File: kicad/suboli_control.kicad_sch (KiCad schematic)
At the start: 41 parts, among them J1 DC barrel jack panel header 5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, J2 3.5 mm TRS input panel header, J3 4-pole Speakon/XLR panel head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, J4 3.5 mm TRS headphone panel he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, SW1 DPST power switch panel header, U1 TLE2426ILP

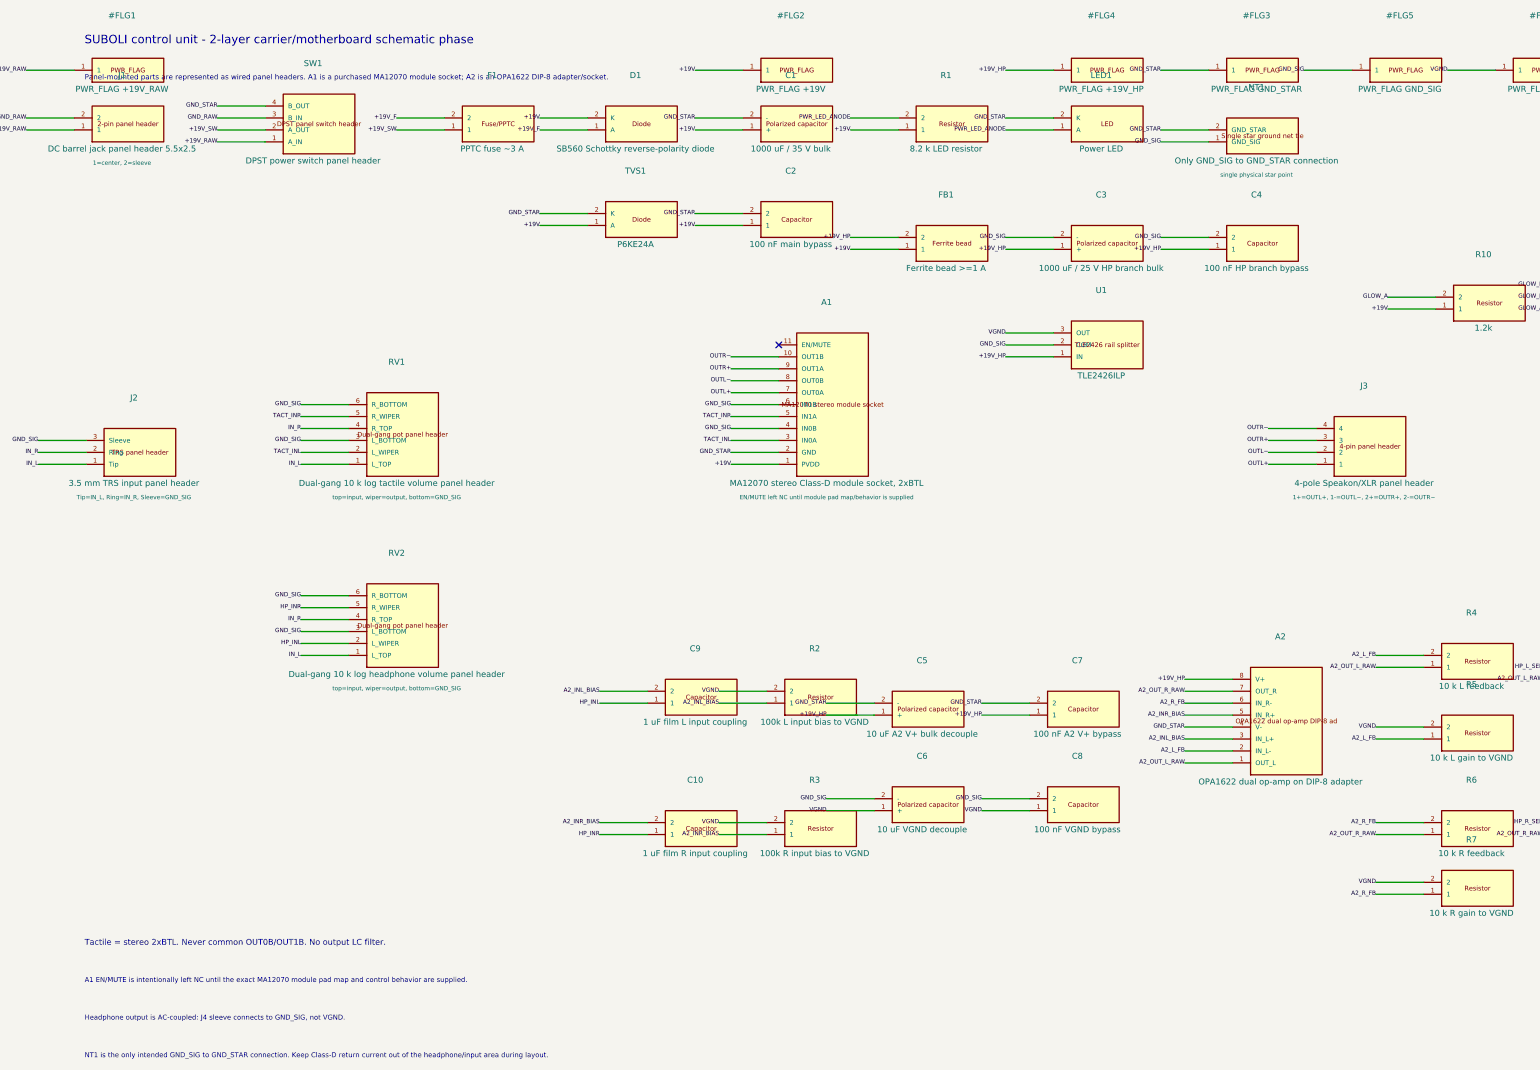
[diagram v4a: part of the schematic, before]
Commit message: R4: MA12070 off-board (stacked), J3+OUT nets removed, J5/J6 added
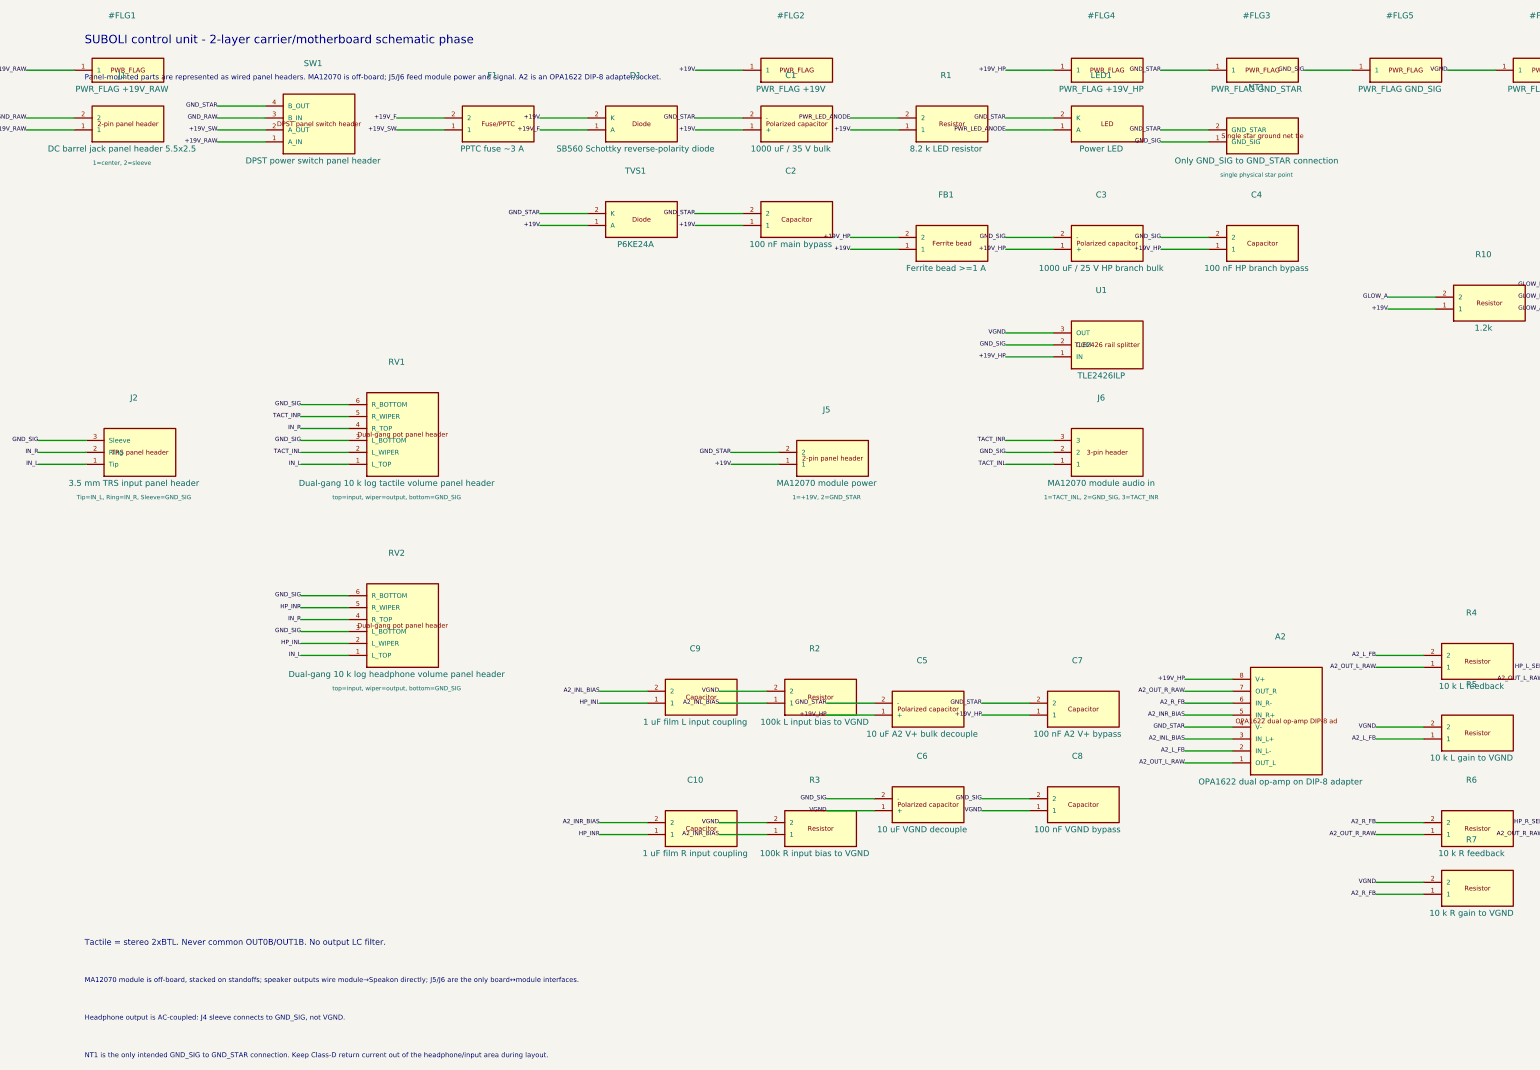
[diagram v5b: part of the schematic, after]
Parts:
- removed A1: MA12070 stereo Class-D module socket, 2xBTL, symbol suboli_control:A1_MA12070_MODULE
- removed J3: 4-pole Speakon/XLR panel header, Connector_Phoenix_MSTB:PhoenixContact_MSTBA_2,5_4-G-5,08_1x04_P5.08mm_Horizontal, symbol suboli_control:CONN_4
- added J5: MA12070 module power, Connector_Phoenix_MSTB:PhoenixContact_MSTBA_2,5_2-G-5,08_1x02_P5.08mm_Horizontal, symbol suboli_control:CONN_2
- added J6: MA12070 module audio in, Connector_JST:JST_XH_B3B-XH-A_1x03_P2.50mm_Vertical, symbol suboli_control:CONN_3
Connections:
- net +19V: now also J5.1
- net GND_SIG: now also J6.2
- net GND_STAR: now also J5.2
- net TACT_INL: now also J6.1
- net TACT_INR: now also J6.3
- no-connect marks 1 -> 0
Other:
- note added: "MA12070 module is off-board, stacked on standoffs; speaker outputs wire module→Speakon directly; J5/J6 are the only board↔module interfaces."
- note added: "Panel-mounted parts are represented as wired panel headers. MA12070 is off-board; J5/J6 feed module power and signal. A2 is an OPA1622 DIP-8 adapter/socket."
- note removed: "A1 EN/MUTE is intentionally left NC until the exact MA12070 module pad map and control behavior are supplied."
- note removed: "Panel-mounted parts are represented as wired panel headers. A1 is a purchased MA12070 module socket; A2 is an OPA1622 DIP-8 adapter/socket."
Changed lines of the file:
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@@
   )
   (text "SUBOLI control unit - 2-layer carrier/motherboard schematic phase" (at 20.00 14.00 0) (effects (font (size 1.80 1.80)) (justify left)))
-  (text "Panel-mounted parts are represented as wired panel headers. A1 is a purchased MA12070 module socket; A2 is an OPA1622 DIP-8 adapter/socket." (at 20.00 22.00 0) (effects (font (size 1.10 1.10)) (justify left)))
+  (text "Panel-mounted parts are represented as wired panel headers. MA12070 is off-board; J5/J6 feed module power and signal. A2 is an OPA1622 DIP-8 adapter/socket." (at 20.00 22.00 0) (effects (font (size 1.10 1.10)) (justify left)))
   (text "Tactile = stereo 2xBTL. Never common OUT0B/OUT1B. No output LC filter." (at 20.00 206.00 0) (effects (font (size 1.25 1.25)) (justify left)))
-  (text "A1 EN/MUTE is intentionally left NC until the exact MA12070 module pad map and control behavior are supplied." (at 20.00 214.00 0) (effects (font (size 1.05 1.05)) (justify left)))
+  (text "MA12070 module is off-board, stacked on standoffs; speaker outputs wire module→Speakon directly; J5/J6 are the only board↔module interfaces." (at 20.00 214.00 0) (effects (font (size 1.05 1.05)) (justify left)))
   (text "Headphone output is AC-coupled: J4 sleeve connects to GND_SIG, not VGND." (at 20.00 222.00 0) (effects (font (size 1.05 1.05)) (justify left)))
   (text "NT1 is the only intended GND_SIG to GND_STAR connection. Keep Class-D return current out of the headphone/input area during layout." (at 20.00 230.00 0) (effects (font (size 1.05 1.05)) (justify left)))
@@
   (label "GND_SIG" (at 66.04 132.08 0) (effects (font (size 0.90 0.90)) (justify right)))
   (symbol
-    (lib_id "suboli_control:A1_MA12070_MODULE")
+    (lib_id "suboli_control:CONN_2")
     (at 177.80 104.14 0)
     (unit 1)
@@
     (on_board yes)
     (dnp no)
-    (property "Reference" "A1" (at 177.80 69.66 0) (effects (font (size 1.27 1.27))))
-    (property "Value" "MA12070 stereo Class-D module socket, 2xBTL" (at 177.80 108.14 0) (effects (font (size 1.27 1.27))))
-    (property "Footprint" "" (at 177.80 104.14 0) (effects (font (size 1.27 1.27)) (hide yes)))
+    (property "Reference" "J5" (at 177.80 92.52 0) (effects (font (size 1.27 1.27))))
+    (property "Value" "MA12070 module power" (at 177.80 108.14 0) (effects (font (size 1.27 1.27))))
+    (property "Footprint" "Connector_Phoenix_MSTB:PhoenixContact_MSTBA_2,5_2-G-5,08_1x02_P5.08mm_Horizontal" (at 177.80 104.14 0) (effects (font (size 1.27 1.27)) (hide yes)))
     (property "Datasheet" "~" (at 177.80 104.14 0) (effects (font (size 1.27 1.27)) (hide yes)))
-    (property "Pending" "EN/MUTE left NC until module pad map/behavior is supplied" (at 177.80 111.14 0) (effects (font (size 0.90 0.90))))
-    (pin "1")
-    (pin "2")
-    (pin "3")
-    (pin "4")
-    (pin "5")
-    (pin "6")
-    (pin "7")
-    (pin "8")
-    (pin "9")
-    (pin "10")
-    (pin "11")
-    (instances
-      (project "suboli_control"
-        (path "/35397207-27a9-5c6b-ad79-7b20c8370a7e"
-          (reference "A1")
+    (property "Supplier" "HESTORE" (at 177.80 104.14 0) (effects (font (size 1.27 1.27)) (hide yes)))
+    (property "Supplier_PN" "100.425.38" (at 177.80 104.14 0) (effects (font (size 1.27 1.27)) (hide yes)))
+    (property "Function" "Stacked module PVDD feed" (at 177.80 104.14 0) (effects (font (size 1.27 1.27)) (hide yes)))
+    (property "Pinout" "1=+19V, 2=GND_STAR" (at 177.80 111.14 0) (effects (font (size 0.90 0.90))))
+    (pin "1")
+    (pin "2")
+    (instances
+      (project "suboli_control"
+        (path "/35397207-27a9-5c6b-ad79-7b20c8370a7e"
+          (reference "J5")
           (unit 1)
         )
@@
   (wire (pts (xy 167.64 101.60) (xy 157.48 101.60)) (stroke (width 0) (type default)))
   (label "GND_STAR" (at 157.48 101.60 0) (effects (font (size 0.90 0.90)) (justify right)))
-  (wire (pts (xy 167.64 99.06) (xy 157.48 99.06)) (stroke (width 0) (type default)))
-  (label "TACT_INL" (at 157.48 99.06 0) (effects (font (size 0.90 0.90)) (justify right)))
-  (wire (pts (xy 167.64 96.52) (xy 157.48 96.52)) (stroke (width 0) (type default)))
-  (label "GND_SIG" (at 157.48 96.52 0) (effects (font (size 0.90 0.90)) (justify right)))
-  (wire (pts (xy 167.64 93.98) (xy 157.48 93.98)) (stroke (width 0) (type default)))
-  (label "TACT_INR" (at 157.48 93.98 0) (effects (font (size 0.90 0.90)) (justify right)))
-  (wire (pts (xy 167.64 91.44) (xy 157.48 91.44)) (stroke (width 0) (type default)))
-  (label "GND_SIG" (at 157.48 91.44 0) (effects (font (size 0.90 0.90)) (justify right)))
-  (wire (pts (xy 167.64 88.90) (xy 157.48 88.90)) (stroke (width 0) (type default)))
-  (label "OUTL+" (at 157.48 88.90 0) (effects (font (size 0.90 0.90)) (justify right)))
-  (wire (pts (xy 167.64 86.36) (xy 157.48 86.36)) (stroke (width 0) (type default)))
-  (label "OUTL−" (at 157.48 86.36 0) (effects (font (size 0.90 0.90)) (justify right)))
-  (wire (pts (xy 167.64 83.82) (xy 157.48 83.82)) (stroke (width 0) (type default)))
-  (label "OUTR+" (at 157.48 83.82 0) (effects (font (size 0.90 0.90)) (justify right)))
-  (wire (pts (xy 167.64 81.28) (xy 157.48 81.28)) (stroke (width 0) (type default)))
-  (label "OUTR−" (at 157.48 81.28 0) (effects (font (size 0.90 0.90)) (justify right)))
-  (symbol
-    (lib_id "suboli_control:CONN_4")
-    (at 292.10 104.14 0)
-    (unit 1)
-    (exclude_from_sim no)
-    (in_bom yes)
-    (on_board yes)
-    (dnp no)
-    (property "Reference" "J3" (at 292.10 87.44 0) (effects (font (size 1.27 1.27))))
-    (property "Value" "4-pole Speakon/XLR panel header" (at 292.10 108.14 0) (effects (font (size 1.27 1.27))))
-    (property "Footprint" "Connector_Phoenix_MSTB:PhoenixContact_MSTBA_2,5_4-G-5,08_1x04_P5.08mm_Horizontal" (at 292.10 104.14 0) (effects (font (size 1.27 1.27)) (hide yes)))
-    (property "Datasheet" "~" (at 292.10 104.14 0) (effects (font (size 1.27 1.27)) (hide yes)))
-    (property "Supplier" "HESTORE" (at 292.10 104.14 0) (effects (font (size 1.27 1.27)) (hide yes)))
-    (property "Supplier_PN" "100.425.40" (at 292.10 104.14 0) (effects (font (size 1.27 1.27)) (hide yes)))
-    (property "Function" "4-pole Speakon/XLR tactile output" (at 292.10 104.14 0) (effects (font (size 1.27 1.27)) (hide yes)))
-    (property "Pinout" "1+=OUTL+, 1-=OUTL−, 2+=OUTR+, 2-=OUTR−" (at 292.10 111.14 0) (effects (font (size 0.90 0.90))))
+  (symbol
+    (lib_id "suboli_control:CONN_3")
+    (at 236.22 104.14 0)
+    (unit 1)
+    (exclude_from_sim no)
+    (in_bom yes)
+    (on_board yes)
+    (dnp no)
+    (property "Reference" "J6" (at 236.22 89.98 0) (effects (font (size 1.27 1.27))))
+    (property "Value" "MA12070 module audio in" (at 236.22 108.14 0) (effects (font (size 1.27 1.27))))
+    (property "Footprint" "Connector_JST:JST_XH_B3B-XH-A_1x03_P2.50mm_Vertical" (at 236.22 104.14 0) (effects (font (size 1.27 1.27)) (hide yes)))
+    (property "Datasheet" "~" (at 236.22 104.14 0) (effects (font (size 1.27 1.27)) (hide yes)))
+    (property "Supplier" "HESTORE" (at 236.22 104.14 0) (effects (font (size 1.27 1.27)) (hide yes)))
+    (property "Supplier_PN" "100.415.50" (at 236.22 104.14 0) (effects (font (size 1.27 1.27)) (hide yes)))
+    (property "Function" "Stacked module signal feed" (at 236.22 104.14 0) (effects (font (size 1.27 1.27)) (hide yes)))
+    (property "Pinout" "1=TACT_INL, 2=GND_SIG, 3=TACT_INR" (at 236.22 111.14 0) (effects (font (size 0.90 0.90))))
     (pin "1")
     (pin "2")
     (pin "3")
-    (pin "4")
-    (instances
-      (project "suboli_control"
-        (path "/35397207-27a9-5c6b-ad79-7b20c8370a7e"
-          (reference "J3")
-          (unit 1)
-        )
-      )
-    )
-  )
-  (wire (pts (xy 281.94 104.14) (xy 271.78 104.14)) (stroke (width 0) (type default)))
-  (label "OUTL+" (at 271.78 104.14 0) (effects (font (size 0.90 0.90)) (justify right)))
-  (wire (pts (xy 281.94 101.60) (xy 271.78 101.60)) (stroke (width 0) (type default)))
-  (label "OUTL−" (at 271.78 101.60 0) (effects (font (size 0.90 0.90)) (justify right)))
-  (wire (pts (xy 281.94 99.06) (xy 271.78 99.06)) (stroke (width 0) (type default)))
-  (label "OUTR+" (at 271.78 99.06 0) (effects (font (size 0.90 0.90)) (justify right)))
-  (wire (pts (xy 281.94 96.52) (xy 271.78 96.52)) (stroke (width 0) (type default)))
-  (label "OUTR−" (at 271.78 96.52 0) (effects (font (size 0.90 0.90)) (justify right)))
+    (instances
+      (project "suboli_control"
+        (path "/35397207-27a9-5c6b-ad79-7b20c8370a7e"
+          (reference "J6")
+          (unit 1)
+        )
+      )
+    )
+  )
+  (wire (pts (xy 226.06 104.14) (xy 215.90 104.14)) (stroke (width 0) (type default)))
+  (label "TACT_INL" (at 215.90 104.14 0) (effects (font (size 0.90 0.90)) (justify right)))
+  (wire (pts (xy 226.06 101.60) (xy 215.90 101.60)) (stroke (width 0) (type default)))
+  (label "GND_SIG" (at 215.90 101.60 0) (effects (font (size 0.90 0.90)) (justify right)))
+  (wire (pts (xy 226.06 99.06) (xy 215.90 99.06)) (stroke (width 0) (type default)))
+  (label "TACT_INR" (at 215.90 99.06 0) (effects (font (size 0.90 0.90)) (justify right)))
   (symbol
     (lib_id "suboli_control:CP_2PIN")
@@
   (wire (pts (xy 320.04 20.32) (xy 309.88 20.32)) (stroke (width 0) (type default)))
   (label "VGND" (at 309.88 20.32 0) (effects (font (size 0.90 0.90)) (justify right)))
-  (no_connect (at 167.64 78.74))
   (sheet_instances
     (path "/"

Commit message: R5: BOM enrichment + C1 footprint fix + design rulebook + PCB capability report
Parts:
- C1: footprint Capacitor_THT:CP_Radial_D12.5mm_P5.00mm -> Capacitor_THT:CP_Radial_D16.0mm_P7.50mm
- J5: Supplier_PN 100.425.38 -> 100.425.63
- LED1: Supplier_PN (none) -> 100.201.14
- RV1, RV2: Supplier_PN (none) -> 100.415.52
- RV3: Supplier_PN (none) -> 100.412.47
- SW1: Supplier_PN 100.425.40 -> 100.425.66
- U1: Supplier_PN (none) -> 100.346.37
